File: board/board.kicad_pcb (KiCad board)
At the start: 2 copper layers, 45 x 13 mm, 14 parts, among them J1 008_USB, J2 008_USB, J3 B0505M-2WR2, U1 ADUM3166, Y1 Crystal_GND24_Small

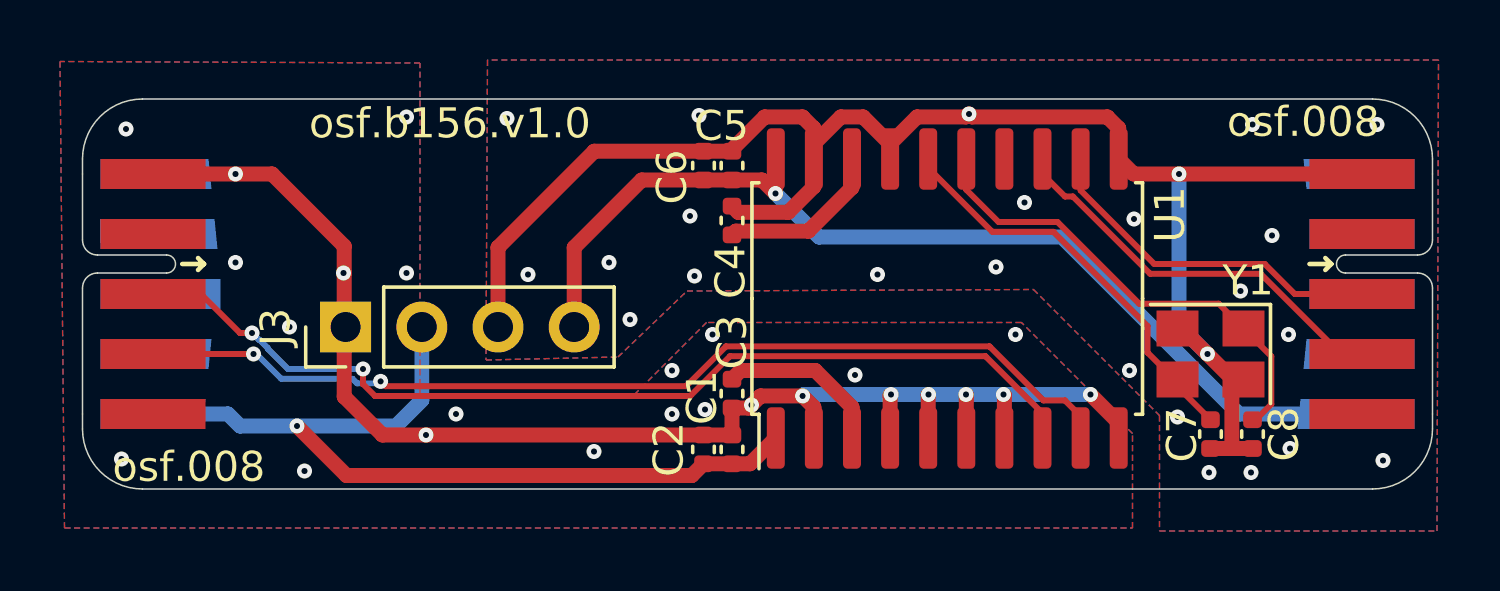
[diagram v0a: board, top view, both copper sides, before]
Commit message: fixed chip package
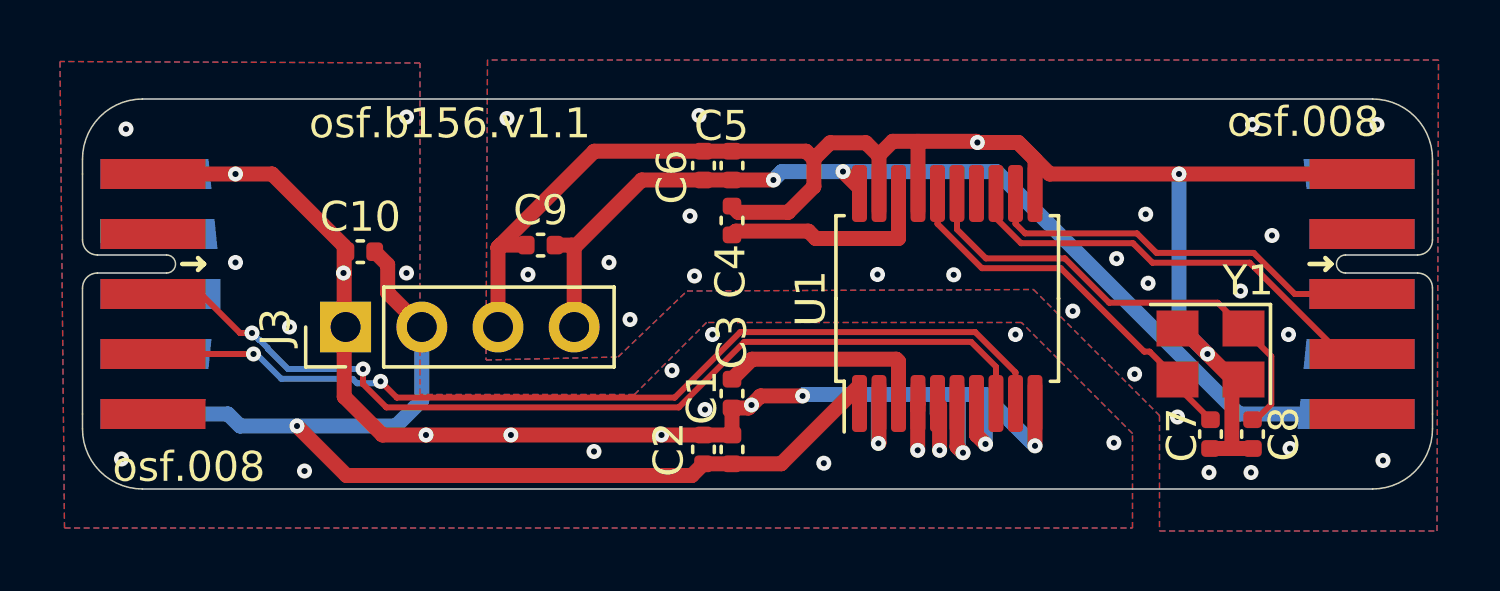
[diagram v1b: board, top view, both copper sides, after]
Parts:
- added C10: 10uF, Capacitor_SMD:C_0402_1005Metric, F.Cu at (149.3, 95.1)
- added C9: 10uF, Capacitor_SMD:C_0402_1005Metric, F.Cu at (155.3, 94.9)
- U1: footprint Package_SO:SOIC-20W_7.5x12.8mm_P1.27mm -> Package_SO:SSOP-20_5.3x7.2mm_P0.65mm
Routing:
- net /dcdc/GND1: track 48.1 -> 57.0 mm, vias 25 -> 27
- net /dcdc/5Vin: track 29.1 -> 35.8 mm
- net /dcdc/GND2: track 55.3 -> 58.9 mm, vias 25 -> 27
- net /iso/D-: track 33.7 -> 31.3 mm
- net /iso/D+: track 33.5 -> 31.8 mm
- net Net-(U1-XI2): track 13.8 -> 12.4 mm
- net /dcdc/5Vout: track 34.1 -> 35.4 mm, vias 1 -> 2
- net /iso/DD+: track 11.9 -> 12.9 mm
- net /iso/VDD1: track 5.65 -> 6.66 mm
- net /iso/VDD2: track 5.60 -> 6.60 mm
- net Net-(U1-XO2): track 15.9 -> 15.3 mm
- net /iso/DD-: track 13.6 -> 14.3 mm
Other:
- board text added: "osf.b156.v1.1"
- board text removed: "osf.b156.v1.0"
